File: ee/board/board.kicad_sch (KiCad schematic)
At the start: 26 parts, among them J1 Lichee_RV_J3, J2 Lichee_RV_J4, J3 USB_A, J4 Conn_01x08_Pin, J5 Conn_01x10_Pin, U1 RTL8723BS, U6 USBLC6-2SC6

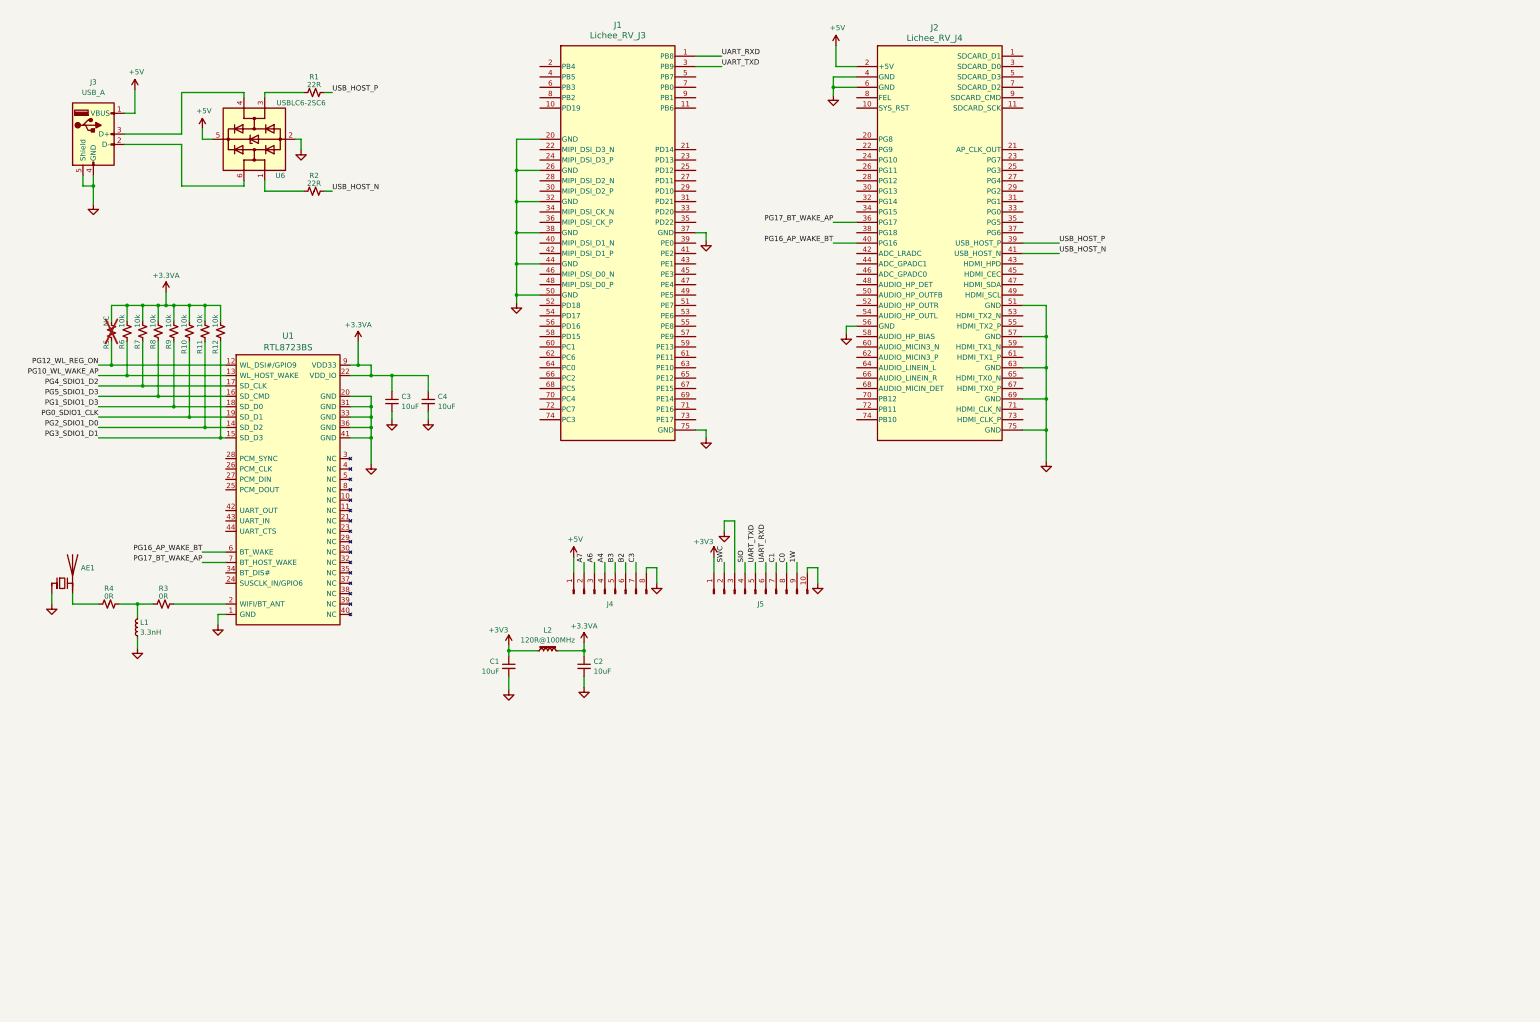
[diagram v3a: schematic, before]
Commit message: Added new wifi module
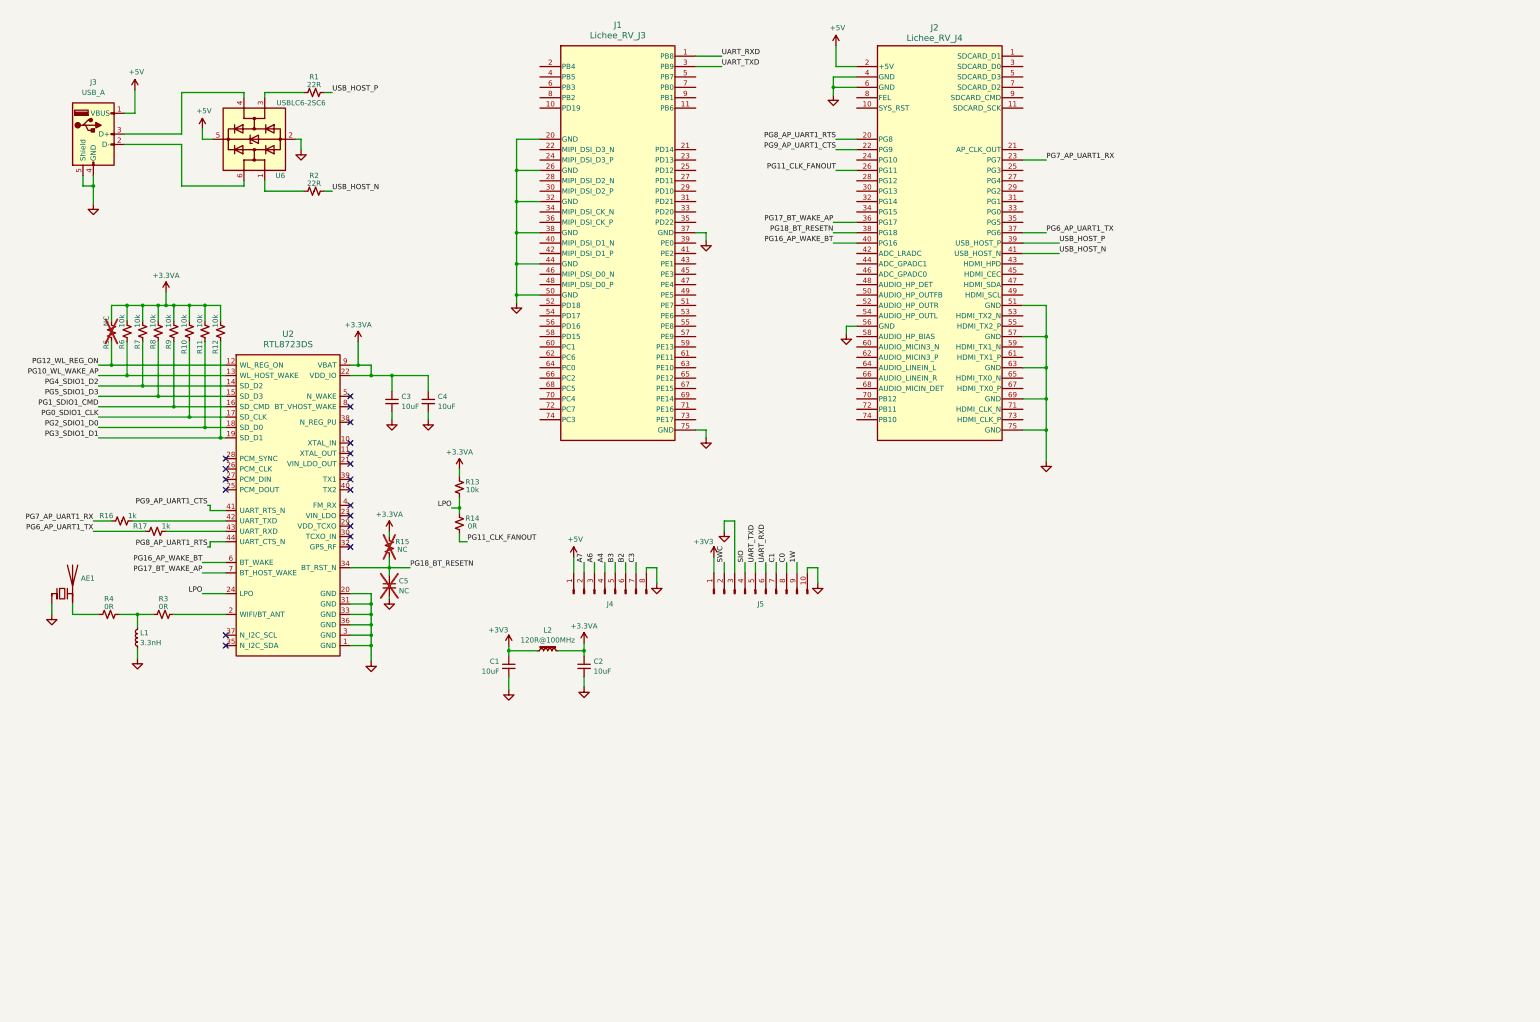
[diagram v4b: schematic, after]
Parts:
- removed U1: RTL8723BS, Omlex_IC:RL-SM02BD(RTL8723BS), symbol olimex:RTL8723BS(ComboModule)
- added C5: NC, symbol Device:C_Small
- added R13: 10k, Resistor_SMD:R_0603_1608Metric, symbol Device:R_Small_US
- added R14: 0R, Resistor_SMD:R_0603_1608Metric, symbol Device:R_Small_US
- added R15: NC, Resistor_SMD:R_0603_1608Metric, symbol Device:R_Small_US
- added R16, R17: 1k, Resistor_SMD:R_0603_1608Metric, symbol Device:R_Small_US
- added U2: RTL8723DS, symbol rtl8723ds:RTL8723DS
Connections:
- net +3.3VA: now also R13.2, R15.2, U2.22 (VDD_IO), U2.9 (VBAT)
- net GND: now also C5.2, U2.1 (GND), U2.20 (GND), U2.3 (GND), U2.31 (GND), U2.33 (GND), U2.36 (GND)
- net PG0_SDIO1_CLK: now also U2.17 (SD_CLK)
- net PG10_WL_WAKE_AP: now also U2.13 (WL_HOST_WAKE)
- net PG12_WL_REG_ON: now also U2.12 (WL_REG_ON)
- net PG16_AP_WAKE_BT: now also U2.6 (BT_WAKE)
- net PG17_BT_WAKE_AP: now also U2.7 (BT_HOST_WAKE)
- net PG2_SDIO1_D0: now also U2.18 (SD_D0)
- net PG3_SDIO1_D1: now also U2.19 (SD_D1)
- net PG4_SDIO1_D2: now also U2.14 (SD_D2)
- net PG5_SDIO1_D3: now also U2.15 (SD_D3)
- net at R3.2: now also U2.2 (WIFI/BT_ANT)
- net PG8_AP_UART1_RTS: now reaches J2.20 (PG8)
- net PG8_AP_UART1_RTS: now also U2.44 (UART_CTS_N)
- net PG9_AP_UART1_CTS: now reaches J2.22 (PG9)
- net PG9_AP_UART1_CTS: now also U2.41 (UART_RTS_N)
- net PG7_AP_UART1_RX: now reaches J2.23 (PG7)
- net PG7_AP_UART1_RX: now also R16.1
- net PG11_CLK_FANOUT: now reaches J2.26 (PG11)
- net PG11_CLK_FANOUT: now also R14.1
- net PG6_AP_UART1_TX: now reaches J2.37 (PG6)
- net PG6_AP_UART1_TX: now also R17.1
- net PG18_BT_RESETN: now reaches J2.38 (PG18)
- net PG18_BT_RESETN: now also C5.1, R15.1, U2.34 (BT_RST_N)
- net PG1_SDIO1_D3 renamed PG1_SDIO1_CMD
- net PG1_SDIO1_CMD: now also U2.16 (SD_CMD)
- new net: R16.2, U2.42 (UART_TXD)
- new net: R17.2, U2.43 (UART_RXD)
- new net LPO: R13.1, R14.2, U2.24 (LPO)
- no-connect marks 0 -> 19
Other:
- moved on the sheet: AE1, L1, R3, R4

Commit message: Schematic mostly finished.
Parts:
- removed AE1: Antenna_Chip, symbol Device:Antenna_Chip
- removed L1: 3.3nH, symbol Device:L_Small
- removed R10, R11, R12, R6, R7, R8, R9: 10k, Resistor_SMD:R_0603_1608Metric, symbol Device:R_Small_US
- removed R5: NC, Resistor_SMD:R_0603_1608Metric, symbol Device:R_Small_US
- added C6, C7: NC, Capacitor_SMD:C_0603_1608Metric, symbol Device:C_Small
- added H1: M2.5 Spacer, KiLib:9774025151R, symbol Mechanical:MountingHole
- added J6: Conn_Coaxial, Connector_Coaxial:SMA_Amphenol_901-143_Horizontal, symbol Connector:Conn_Coaxial
- added JP1, JP2, JP3: SolderJumper_2_Bridged, Jumper:SolderJumper-2_P1.3mm_Bridged2Bar_RoundedPad1.0x1.5mm, symbol Jumper:SolderJumper_2_Bridged
- added R18: 10K, Resistor_SMD:R_0603_1608Metric, symbol Device:R_Small_US
- added R19: 100R, Resistor_SMD:R_0603_1608Metric, symbol Device:R_Small_US
- added RN1, RN2: 10k, Resistor_SMD:R_Array_Convex_4x0402, symbol Device:R_Pack04
- added RN5, RN6, RN7: 22R, Resistor_SMD:R_Array_Convex_4x0402, symbol Device:R_Pack04
- added SW1: SW_Push, symbol Switch:SW_Push
- C1, C2, C3, C4, C5: footprint (none) -> Capacitor_SMD:C_0603_1608Metric
- J1, J2: footprint 2199119-5:CONN75_2199119-5_TEC -> 2199119-5:CONN75_2199230-3
- R14: now not fitted
- R15: value NC -> 100K; now fitted
- R4: value 0R -> 100K; now not fitted
- U2: footprint (none) -> KiLib:RTL8723
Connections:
- net +3.3VA: now also RN1.5 (R4.2), RN1.6 (R3.2), RN1.7 (R2.2), RN1.8 (R1.2), RN2.5 (R4.2), RN2.6 (R3.2), RN2.7 (R2.2), RN2.8 (R1.2)
- net GND: now also R4.1, C6.2, C7.2, J6.2 (Ext), R18.1, SW1.1
- net PG0_SDIO1_CLK: now also J2.33 (PG0), RN1.3 (R3.1)
- net PG10_WL_WAKE_AP: now also J2.24 (PG10), RN2.3 (R3.1)
- net PG12_WL_REG_ON: now also J2.28 (PG12), R18.2, RN2.4 (R4.1)
- net PG16_AP_WAKE_BT: now also R4.2
- net PG18_BT_RESETN: now also JP1.2 (B); no longer C5.1, R15.1, U2.34 (BT_RST_N)
- net PG1_SDIO1_CMD: now also J2.31 (PG1), RN1.4 (R4.1)
- net PG2_SDIO1_D0: now also J2.29 (PG2), RN1.2 (R2.1)
- net PG3_SDIO1_D1: now also J2.25 (PG3), RN1.1 (R1.1)
- net PG4_SDIO1_D2: now also J2.27 (PG4), RN2.2 (R2.1)
- net PG5_SDIO1_D3: now also J2.35 (PG5), RN2.1 (R1.1)
- net UART_RXD: now also JP2.2 (B); no longer J1.1 (PB8)
- net UART_TXD: now also JP3.2 (B); no longer J1.3 (PB9)
- net at R3.1: now also C7.1, J6.1 (In); no longer R4.2
- net at J1.39 (PE0): now also RN5.4 (R4.1)
- net at J1.41 (PE2): now also RN5.3 (R3.1)
- net at J1.43 (PE1): now also RN5.2 (R2.1)
- net RMII_TXCK: now reaches J1.45 (PE3)
- net RMII_TXCK: now also RN7.3 (R3.1)
- net at J1.47 (PE4): now also RN5.1 (R1.1)
- net at J1.49 (PE5): now also RN6.4 (R4.1)
- net at J1.51 (PE7): now also RN6.3 (R3.1)
- net at J1.53 (PE6): now also RN6.2 (R2.1)
- net at J1.55 (PE8): now also RN6.1 (R1.1)
- net at J1.57 (PE9): now also RN7.4 (R4.1)
- net at J1.71 (PE16): now also RN7.2 (R2.1)
- net at J2.10 (SYS_RST): now also R19.1
- net at R3.2, U2.2 (WIFI/BT_ANT): now also C6.1
- new net: C5.1, JP1.1 (A), R15.1, U2.34 (BT_RST_N)
- new net: R19.2, SW1.2
- new net: J1.1 (PB8), JP2.1 (A)
- new net: J1.3 (PB9), JP3.1 (A)
- new net Ethernet/RMII_CRS_DV: RN5.5 (R4.2)
- new net Ethernet/RMII_MDC: RN6.8 (R1.2)
- new net Ethernet/RMII_MDIO: RN7.5 (R4.2)
- new net Ethernet/RMII_RST: RN7.7 (R2.2)
- new net Ethernet/RMII_RXD0: RN5.7 (R2.2)
- new net Ethernet/RMII_RXD1: RN5.6 (R3.2)
- new net Ethernet/RMII_RXER: RN6.6 (R3.2)
- new net Ethernet/RMII_TXCK: RN7.6 (R3.2)
- new net Ethernet/RMII_TXD0: RN5.8 (R1.2)
- new net Ethernet/RMII_TXD1: RN6.5 (R4.2)
- new net Ethernet/RMII_TXEN: RN6.7 (R2.2)
- no-connect marks 19 -> 18
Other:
- added sheet Ethernet (ethernet.kicad_sch)
- note added: "50Ω"
- note added: "?"
- note added: "A"
- note added: "B"
- note added: "C"
- note added: "D"
- note added: "Notes ----- - Switch to power device from Flipper or USB? Can you do this with a diode?"
- note added: "RTL8723DS - Populate B and D XR829 - Populate A and C"
- moved on the sheet: C3, C4, J1, R3

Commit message: Moved some of the local library stuff into the submodule.
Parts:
- J1, J2: footprint 2199119-5:CONN75_2199230-3 -> KiLib:CONN75_2199230-3
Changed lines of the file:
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@@
       (effects (font (size 1.524 1.524)))
     )
-    (property "Footprint" "2199119-5:CONN75_2199230-3" (at 137.795 20.955 0)
+    (property "Footprint" "KiLib:CONN75_2199230-3" (at 137.795 20.955 0)
       (effects (font (size 1.27 1.27) italic) hide)
     )
@@
       (effects (font (size 1.524 1.524)))
     )
-    (property "Footprint" "2199119-5:CONN75_2199230-3" (at 238.76 23.495 0)
+    (property "Footprint" "KiLib:CONN75_2199230-3" (at 238.76 23.495 0)
       (effects (font (size 1.27 1.27) italic) hide)
     )

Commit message: Nearly finished routing.
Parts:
- J1, J2: MPN 2199119-5 -> 2199230-3
- L2: footprint (none) -> Inductor_SMD:L_0805_2012Metric; MPN (none) -> MMZ2012R121AT000
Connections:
- net Ethernet/RMII_CRS_DV: now also RN5.8 (R1.2); no longer RN5.5 (R4.2)
- net Ethernet/RMII_MDC: now also RN7.8 (R1.2); no longer RN6.8 (R1.2)
- net Ethernet/RMII_MDIO: now also RN7.7 (R2.2); no longer RN7.5 (R4.2)
- net Ethernet/RMII_RST: now also RN7.6 (R3.2); no longer RN7.7 (R2.2)
- net Ethernet/RMII_RXD0: now also RN5.6 (R3.2); no longer RN5.7 (R2.2)
- net Ethernet/RMII_RXD1: now also RN5.7 (R2.2); no longer RN5.6 (R3.2)
- net Ethernet/RMII_TXCK: now also RN5.5 (R4.2); no longer RN7.6 (R3.2)
- net Ethernet/RMII_TXD0: now also RN6.8 (R1.2); no longer RN5.8 (R1.2)
- net Ethernet/RMII_TXD1: now also RN6.7 (R2.2); no longer RN6.5 (R4.2)
- net Ethernet/RMII_TXEN: now also RN6.5 (R4.2); no longer RN6.7 (R2.2)
- net at U6.1 (I/O1): now also R1.1; no longer R2.1
- net at U6.3 (I/O2): now also R2.1; no longer R1.1
- net at U6.4 (I/O2): now also J3.2 (D-); no longer J3.3 (D+)
- net at U6.6 (I/O1): now also J3.3 (D+); no longer J3.2 (D-)
- net at RN6.1 (R1.1): now also J1.47 (PE4); no longer J1.55 (PE8)
- net at RN6.2 (R2.1): now also J1.49 (PE5); no longer J1.53 (PE6)
- net at RN6.4 (R4.1): now also J1.53 (PE6); no longer J1.49 (PE5)
- net at RN5.1 (R1.1): now also J1.39 (PE0); no longer J1.47 (PE4)
- net at RN5.2 (R2.1): now also J1.41 (PE2); no longer J1.43 (PE1)
- net at RN5.3 (R3.1): now also J1.43 (PE1); no longer J1.41 (PE2)
- net at RN5.4 (R4.1): now also J1.45 (PE3); no longer J1.39 (PE0)
- net at RN7.1 (R1.1): now also J1.55 (PE8)
- net at RN7.2 (R2.1): now also J1.57 (PE9); no longer J1.71 (PE16)
- net at RN7.4 (R4.1): no longer J1.57 (PE9)
- net RMII_TXCK: no longer names the net of RN7.3 (R3.1)
- net RMII_TXCK: now also J1.71 (PE16); no longer J1.45 (PE3)
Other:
- moved on the sheet: RN5, RN6, RN7

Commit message: Finished R1
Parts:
- C1, C2, C3, C4: MPN (none) -> LMK107BBJ106MALT
- C5, C6, C7, R14, R18, R4: now left out of the parts list
- R1, R2: MPN (none) -> RC0603FR-1322RL
- R13: MPN (none) -> RC0603FR-1310KL
- R15, R19: MPN (none) -> RC0603FR-13100KL
- R16, R17: MPN (none) -> RC0603FR-131KL
- R3: MPN (none) -> RC0603FR-130RL
- SW1: footprint (none) -> Button_Switch_SMD:SW_SPST_PTS645; MPN (none) -> PTS645SH43SMTR92 LFS
- U2: MPN (none) -> RTL8723DS
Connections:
- net GND: now also J1.76 (SHD), J1.77 (SHD), J2.76 (SHD), J2.77 (SHD)
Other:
- moved on the sheet: R19
